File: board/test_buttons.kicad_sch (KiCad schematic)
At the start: 22 parts, among them SW11 SW_Wuerth_450301014042, SW12 SW_Wuerth_450301014042, SW13 SW_Wuerth_450301014042, SW14 SW_Wuerth_450301014042, SW15 SW_Wuerth_450301014042, SW16 SW_Wuerth_450301014042, SW4 SW_Push, SW6 SW_Push, SW7 SW_Push, SW8 SW_Push

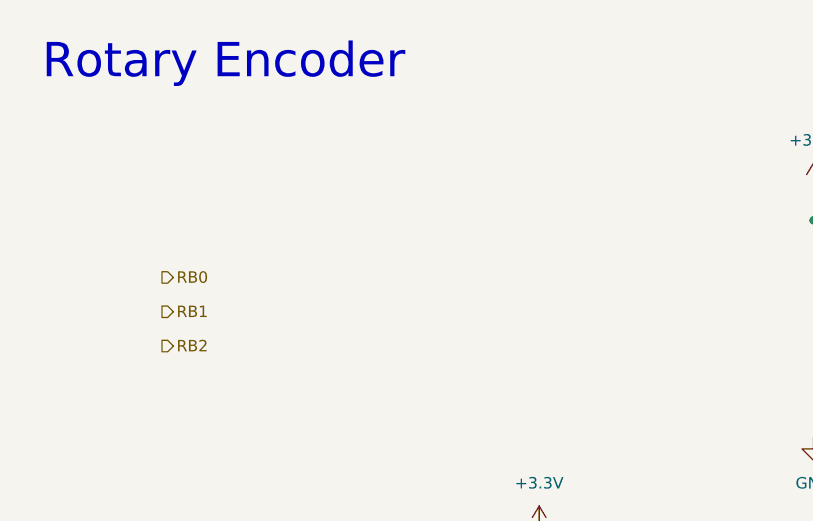
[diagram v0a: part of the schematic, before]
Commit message: Added Rotary Encoder
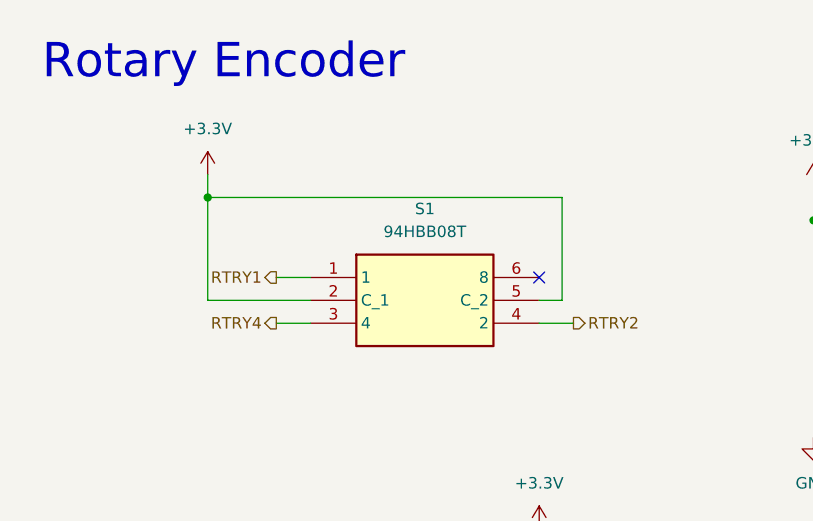
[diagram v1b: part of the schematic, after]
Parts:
- added S1: 94HBB08T, DIPS762W56P254L991H597Q6N, symbol CoreBoard:94HBB08T
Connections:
- net +3.3V: now also S1.2 (C_1), S1.5 (C_2)
- new net RTRY1: S1.1
- new net RTRY2: S1.4 (2)
- new net RTRY4: S1.3 (4)
- no-connect marks 0 -> 1

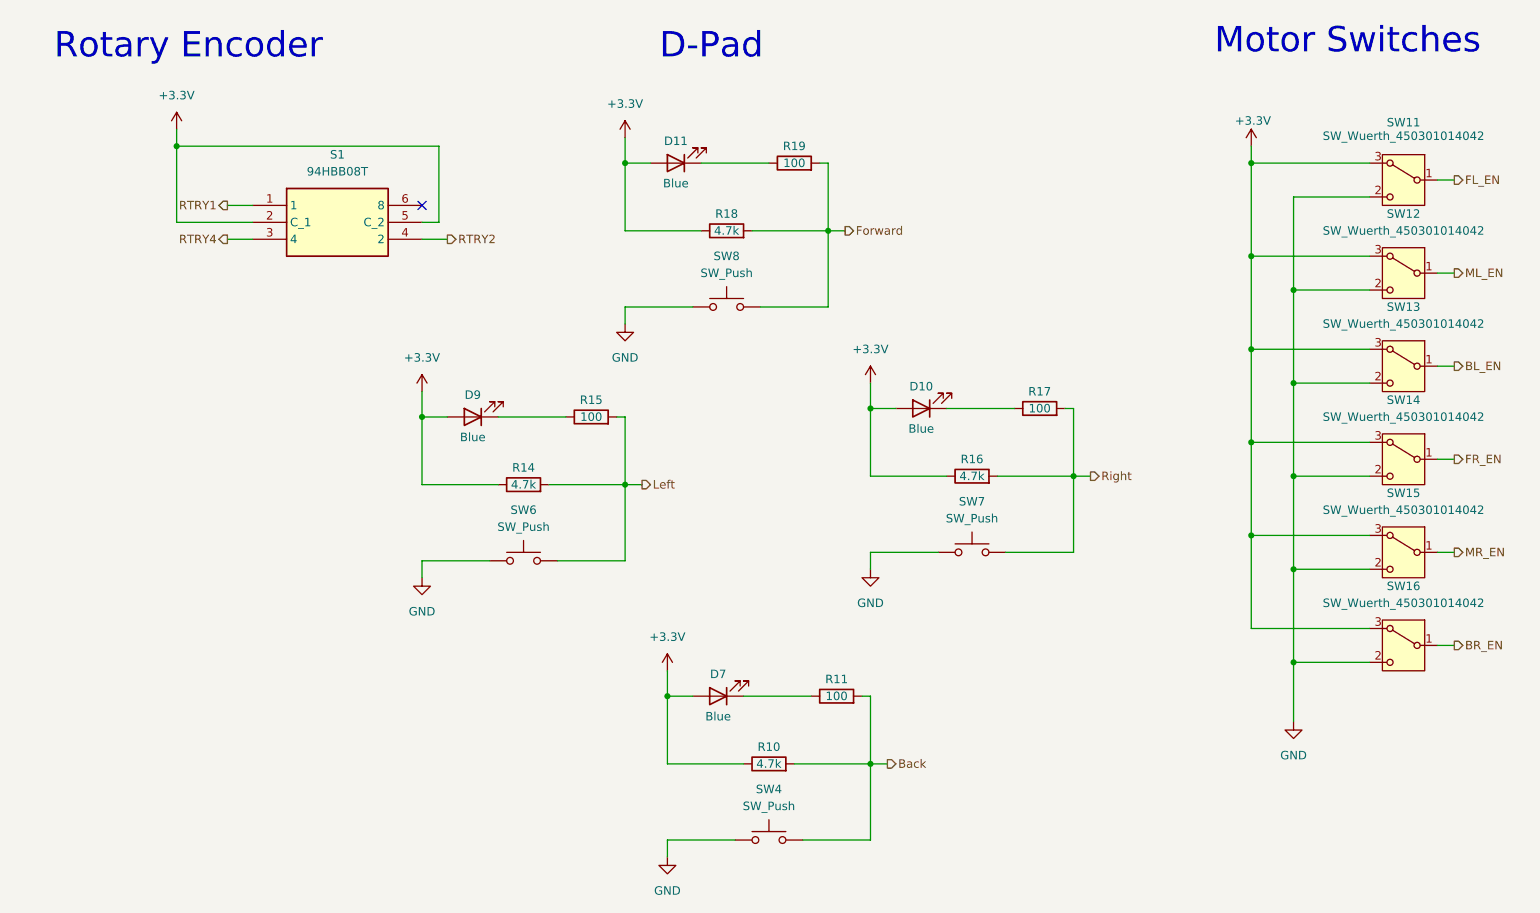
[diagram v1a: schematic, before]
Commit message: Added most Footprints, Schematic review touch up
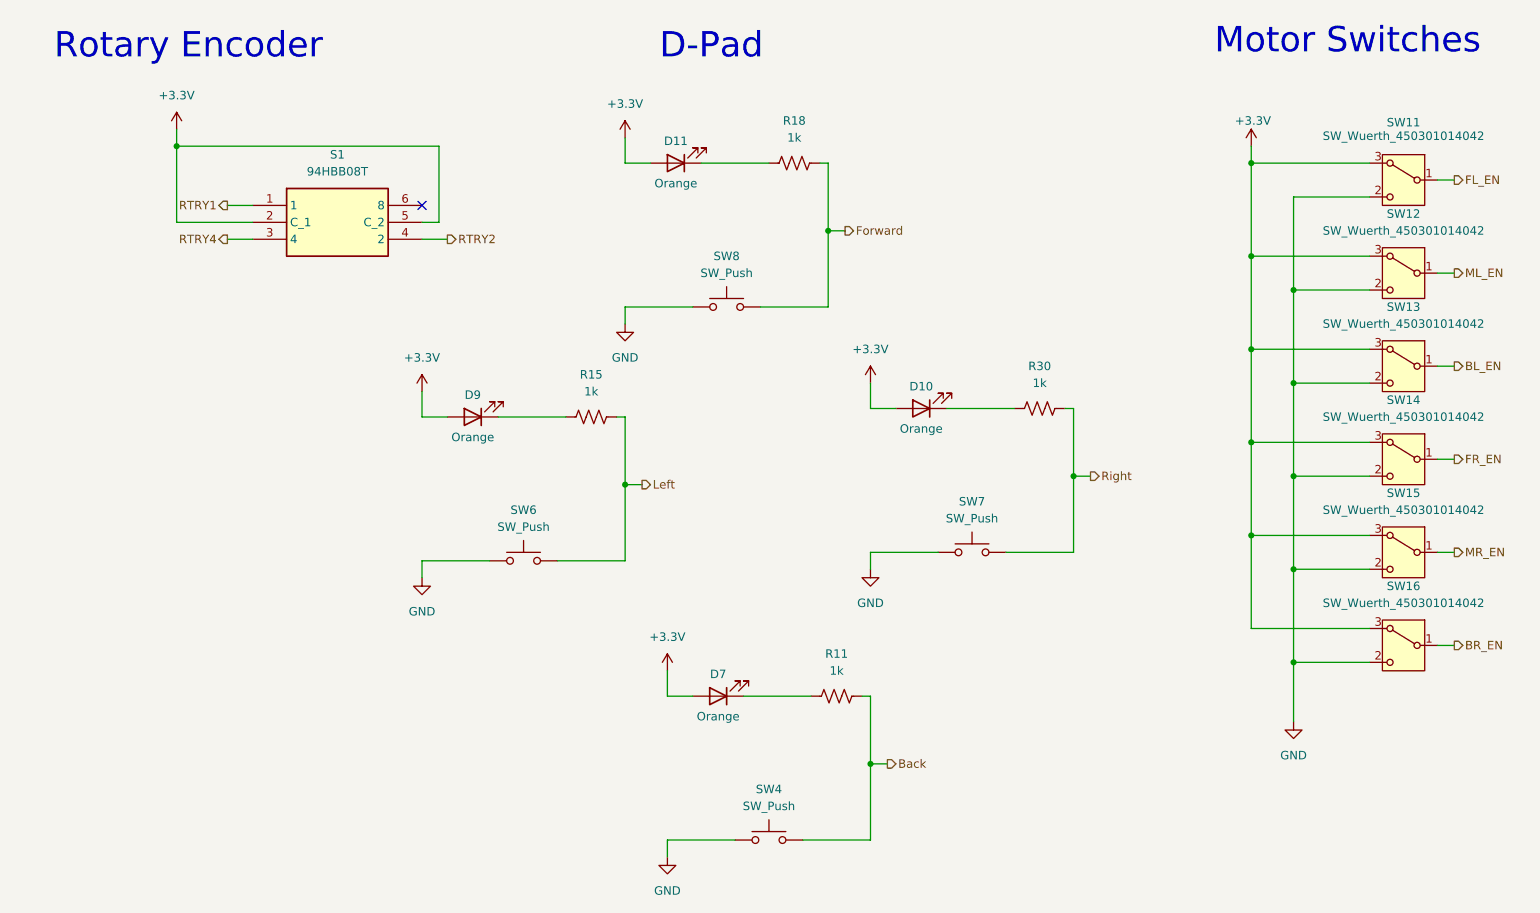
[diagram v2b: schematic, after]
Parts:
- removed R10, R14, R16, R18: 4.7k, Resistor_SMD:R_0603_1608Metric_Pad0.98x0.95mm_HandSolder, symbol Device:R
- removed R11, R15, R17, R19: 100, Resistor_SMD:R_0603_1608Metric_Pad0.98x0.95mm_HandSolder, symbol Device:R
- added R11, R15, R18, R30: 1k, Resistor_SMD:R_0603_1608Metric_Pad0.98x0.95mm_HandSolder, symbol Device:R_US
- D10, D11, D7, D9: value Blue -> Orange
- S1: footprint DIPS762W56P254L991H597Q6N -> (none)
- SW11, SW12, SW13, SW14, SW15, SW16: footprint MRDT_Switches:SW_Switch_03_STSSS9121_Through_Hole -> Button_Switch_THT:SW_Slide-03_Wuerth-WS-SLTV_10x2.5x6.4_P2.54mm
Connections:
- net Back: now also R11.1
- net Forward: now also R18.1
- net Left: now also R15.1
- net Right: now also R30.1
- net at D11.1 (K): now also R18.2
- net at D9.1 (K): now also R15.2
- net at D10.1 (K): now also R30.2
- net at D7.1 (K): now also R11.2

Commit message: added 3d model for rotary encoder
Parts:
- S1: footprint (none) -> CoreBoard:DIPS762W56P254L991H597Q6N
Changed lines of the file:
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@@
 			)
 		)
-		(property "Footprint" ""
+		(property "Footprint" "CoreBoard:DIPS762W56P254L991H597Q6N"
 			(at 85.09 146.99 0)
 			(effects
